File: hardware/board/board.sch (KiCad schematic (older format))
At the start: 64 parts, among them J1 Power, J10 OUT B3, J12 IN C, J13 OUT C1, J14 OUT C2, J15 OUT C3, J17 OUT D, J18 IN D1, J19 IN D2, J2 IN A, J20 IN D3, J3 OUT A1, J4 OUT A2, J5 OUT A3, J7 IN B, J8 OUT B1, J9 OUT B2, U1 OPA4991, U2 OPA4991, U4 OPA4991, U6 OPA4991

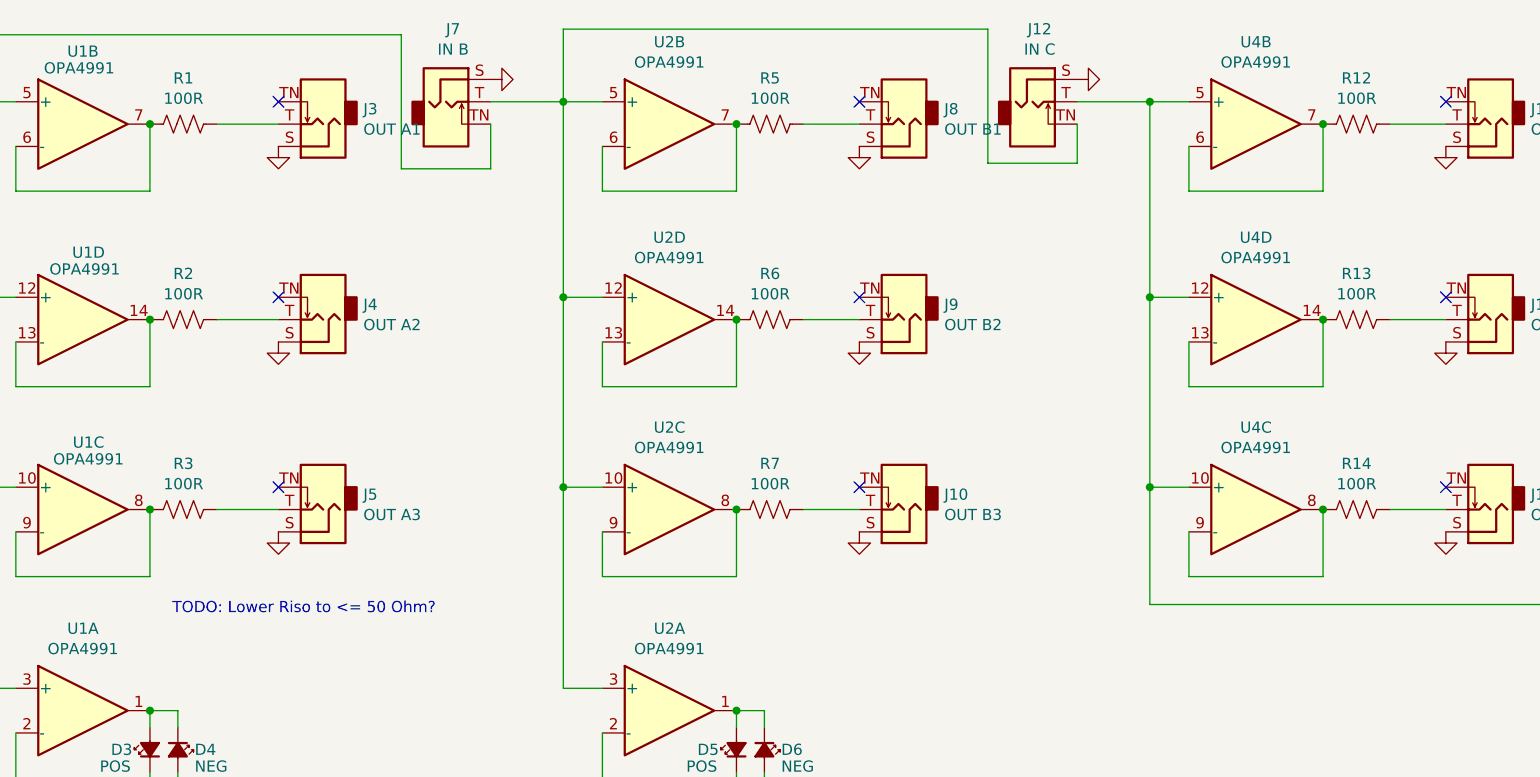
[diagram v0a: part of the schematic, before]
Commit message: Update resistor values; create PDF
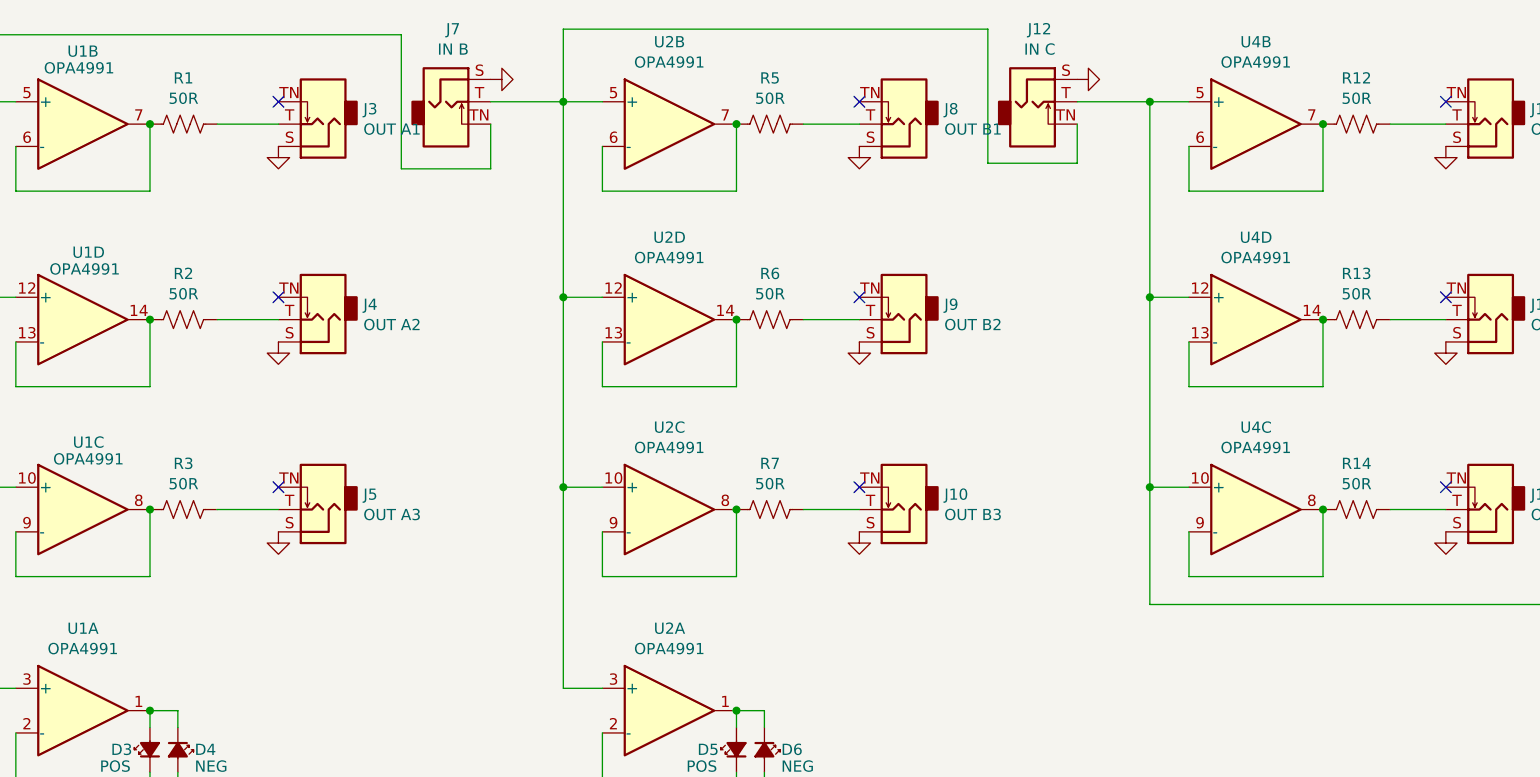
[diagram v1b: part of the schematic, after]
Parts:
- R1, R12, R13, R14, R2, R3, R5, R6, R7: value 100R -> 50R; Notes thin film -> thin film, highest possible wattage for size; mpn R0816P-101-D -> (none)
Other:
- note removed: "TODO: Lower Riso to <= 50 Ohm?"
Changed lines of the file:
@@
 P 2075 975
 F 0 "R1" V 1870 975 50  0000 C CNN
-F 1 "100R" V 1961 975 50  0000 C CNN
+F 1 "50R" V 1961 975 50  0000 C CNN
 F 2 "Resistor_SMD:R_0603_1608Metric_Pad0.98x0.95mm_HandSolder" V 2115 965 50  0001 C CNN
 F 3 "~" H 2075 975 50  0001 C CNN
-F 4 "R0816P-101-D" H 2075 975 50  0001 C CNN "mpn"
-F 5 "thin film" H 2075 975 50  0001 C CNN "Notes"
+F 4 "" H 2075 975 50  0001 C CNN "mpn"
+F 5 "thin film, highest possible wattage for size" H 2075 975 50  0001 C CNN "Notes"
 	1    2075 975
 	0    1    1    0
@@
 P 2075 1850
 F 0 "R2" V 1870 1850 50  0000 C CNN
-F 1 "100R" V 1961 1850 50  0000 C CNN
+F 1 "50R" V 1961 1850 50  0000 C CNN
 F 2 "Resistor_SMD:R_0603_1608Metric_Pad0.98x0.95mm_HandSolder" V 2115 1840 50  0001 C CNN
 F 3 "~" H 2075 1850 50  0001 C CNN
-F 4 "R0816P-101-D" H 2075 1850 50  0001 C CNN "mpn"
-F 5 "thin film" H 2075 1850 50  0001 C CNN "Notes"
+F 4 "" H 2075 1850 50  0001 C CNN "mpn"
+F 5 "thin film, highest possible wattage for size" H 2075 1850 50  0001 C CNN "Notes"
 	1    2075 1850
 	0    1    1    0
@@
 P 2075 2700
 F 0 "R3" V 1870 2700 50  0000 C CNN
-F 1 "100R" V 1961 2700 50  0000 C CNN
+F 1 "50R" V 1961 2700 50  0000 C CNN
 F 2 "Resistor_SMD:R_0603_1608Metric_Pad0.98x0.95mm_HandSolder" V 2115 2690 50  0001 C CNN
 F 3 "~" H 2075 2700 50  0001 C CNN
-F 4 "R0816P-101-D" H 2075 2700 50  0001 C CNN "mpn"
-F 5 "thin film" H 2075 2700 50  0001 C CNN "Notes"
+F 4 "" H 2075 2700 50  0001 C CNN "mpn"
+F 5 "thin film, highest possible wattage for size" H 2075 2700 50  0001 C CNN "Notes"
 	1    2075 2700
 	0    1    1    0
@@
 P 4700 975
 F 0 "R5" V 4495 975 50  0000 C CNN
-F 1 "100R" V 4586 975 50  0000 C CNN
+F 1 "50R" V 4586 975 50  0000 C CNN
 F 2 "Resistor_SMD:R_0603_1608Metric_Pad0.98x0.95mm_HandSolder" V 4740 965 50  0001 C CNN
 F 3 "~" H 4700 975 50  0001 C CNN
-F 4 "R0816P-101-D" H 4700 975 50  0001 C CNN "mpn"
-F 5 "thin film" H 4700 975 50  0001 C CNN "Notes"
+F 4 "" H 4700 975 50  0001 C CNN "mpn"
+F 5 "thin film, highest possible wattage for size" H 4700 975 50  0001 C CNN "Notes"
 	1    4700 975
 	0    1    1    0
@@
 P 4700 1850
 F 0 "R6" V 4495 1850 50  0000 C CNN
-F 1 "100R" V 4586 1850 50  0000 C CNN
+F 1 "50R" V 4586 1850 50  0000 C CNN
 F 2 "Resistor_SMD:R_0603_1608Metric_Pad0.98x0.95mm_HandSolder" V 4740 1840 50  0001 C CNN
 F 3 "~" H 4700 1850 50  0001 C CNN
-F 4 "R0816P-101-D" H 4700 1850 50  0001 C CNN "mpn"
-F 5 "thin film" H 4700 1850 50  0001 C CNN "Notes"
+F 4 "" H 4700 1850 50  0001 C CNN "mpn"
+F 5 "thin film, highest possible wattage for size" H 4700 1850 50  0001 C CNN "Notes"
 	1    4700 1850
 	0    1    1    0
@@
 P 4700 2700
 F 0 "R7" V 4495 2700 50  0000 C CNN
-F 1 "100R" V 4586 2700 50  0000 C CNN
+F 1 "50R" V 4586 2700 50  0000 C CNN
 F 2 "Resistor_SMD:R_0603_1608Metric_Pad0.98x0.95mm_HandSolder" V 4740 2690 50  0001 C CNN
 F 3 "~" H 4700 2700 50  0001 C CNN
-F 4 "R0816P-101-D" H 4700 2700 50  0001 C CNN "mpn"
-F 5 "thin film" H 4700 2700 50  0001 C CNN "Notes"
+F 4 "" H 4700 2700 50  0001 C CNN "mpn"
+F 5 "thin film, highest possible wattage for size" H 4700 2700 50  0001 C CNN "Notes"
 	1    4700 2700
 	0    1    1    0
@@
 P 7325 975
 F 0 "R12" V 7120 975 50  0000 C CNN
-F 1 "100R" V 7211 975 50  0000 C CNN
+F 1 "50R" V 7211 975 50  0000 C CNN
 F 2 "Resistor_SMD:R_0603_1608Metric_Pad0.98x0.95mm_HandSolder" V 7365 965 50  0001 C CNN
 F 3 "~" H 7325 975 50  0001 C CNN
-F 4 "R0816P-101-D" H 7325 975 50  0001 C CNN "mpn"
-F 5 "thin film" H 7325 975 50  0001 C CNN "Notes"
+F 4 "" H 7325 975 50  0001 C CNN "mpn"
+F 5 "thin film, highest possible wattage for size" H 7325 975 50  0001 C CNN "Notes"
 	1    7325 975
 	0    1    1    0
@@
 P 7325 1850
 F 0 "R13" V 7120 1850 50  0000 C CNN
-F 1 "100R" V 7211 1850 50  0000 C CNN
+F 1 "50R" V 7211 1850 50  0000 C CNN
 F 2 "Resistor_SMD:R_0603_1608Metric_Pad0.98x0.95mm_HandSolder" V 7365 1840 50  0001 C CNN
 F 3 "~" H 7325 1850 50  0001 C CNN
-F 4 "R0816P-101-D" H 7325 1850 50  0001 C CNN "mpn"
-F 5 "thin film" H 7325 1850 50  0001 C CNN "Notes"
+F 4 "" H 7325 1850 50  0001 C CNN "mpn"
+F 5 "thin film, highest possible wattage for size" H 7325 1850 50  0001 C CNN "Notes"
 	1    7325 1850
 	0    1    1    0
@@
 P 7325 2700
 F 0 "R14" V 7120 2700 50  0000 C CNN
-F 1 "100R" V 7211 2700 50  0000 C CNN
+F 1 "50R" V 7211 2700 50  0000 C CNN
 F 2 "Resistor_SMD:R_0603_1608Metric_Pad0.98x0.95mm_HandSolder" V 7365 2690 50  0001 C CNN
 F 3 "~" H 7325 2700 50  0001 C CNN
-F 4 "R0816P-101-D" H 7325 2700 50  0001 C CNN "mpn"
-F 5 "thin film" H 7325 2700 50  0001 C CNN "Notes"
+F 4 "" H 7325 2700 50  0001 C CNN "mpn"
+F 5 "thin film, highest possible wattage for size" H 7325 2700 50  0001 C CNN "Notes"
 	1    7325 2700
 	0    1    1    0
@@
 	3325 6800 3175 6800
 Connection ~ 3325 6800
-Text Notes 2025 3175 0    50   ~ 0
-TODO: Lower Riso to <= 50 Ohm?
 Text Notes 8400 5550 0    50   ~ 0
 C11 creates a low-pass filter\n- Fc @ 132kHz w/ 12pF\n- Fc @ 88kHz w/ 18pF

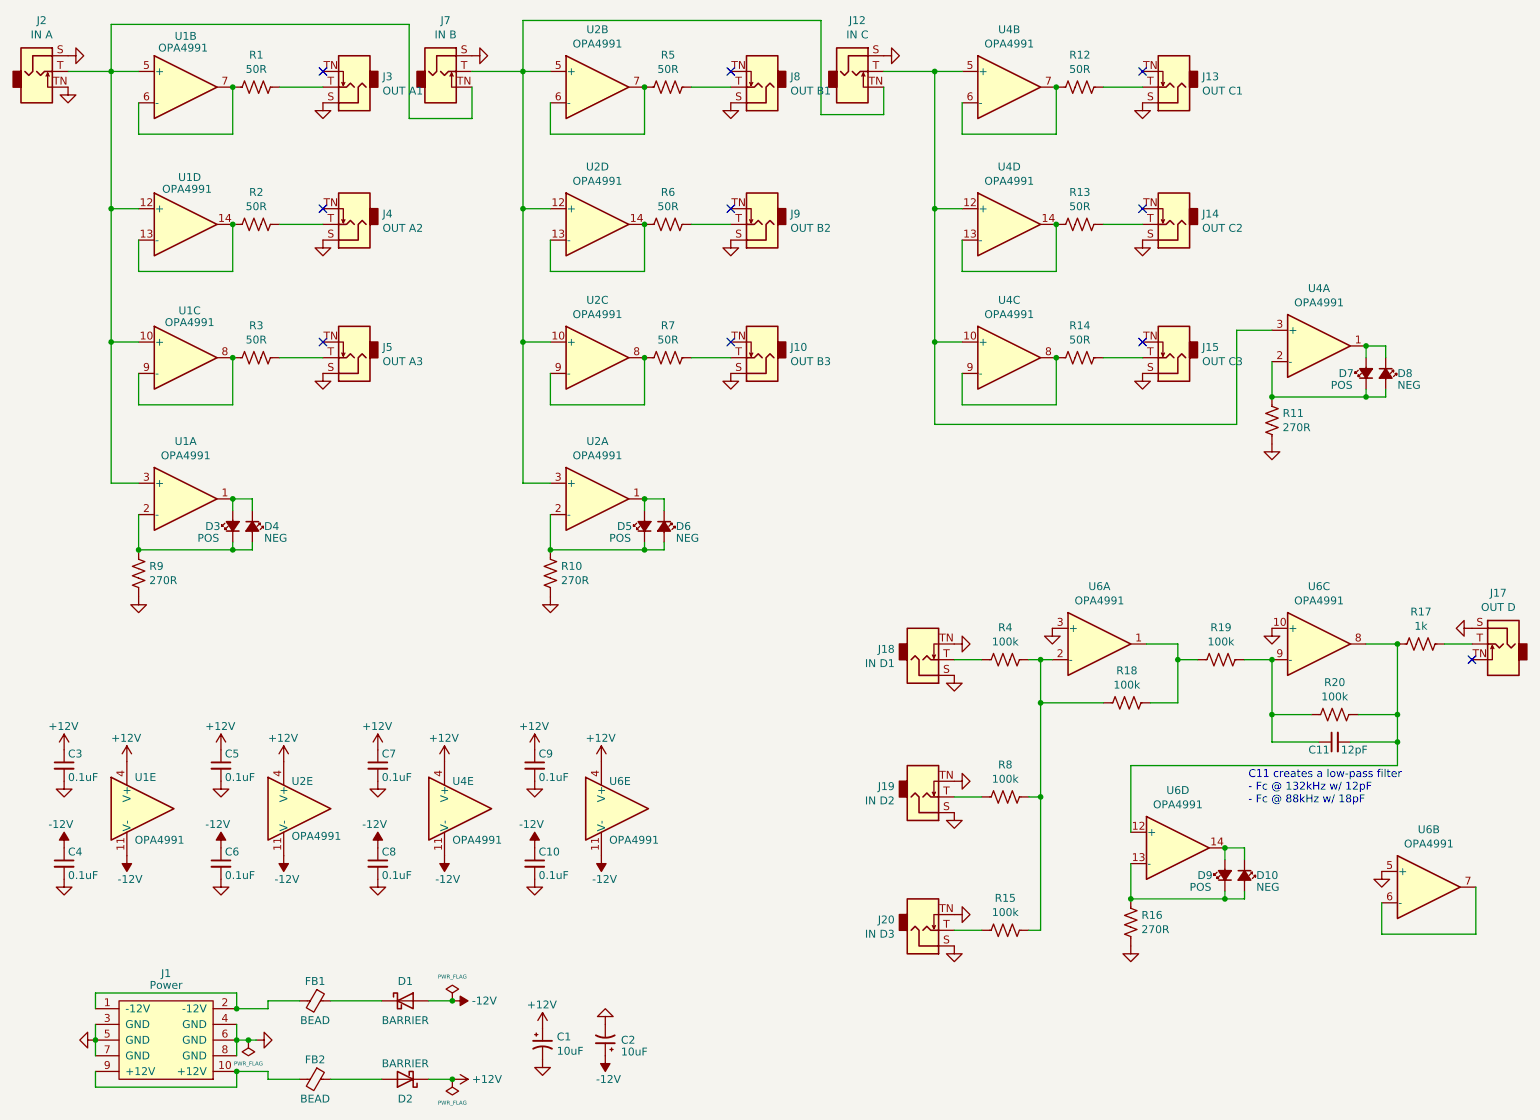
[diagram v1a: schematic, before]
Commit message: Update values for resistors
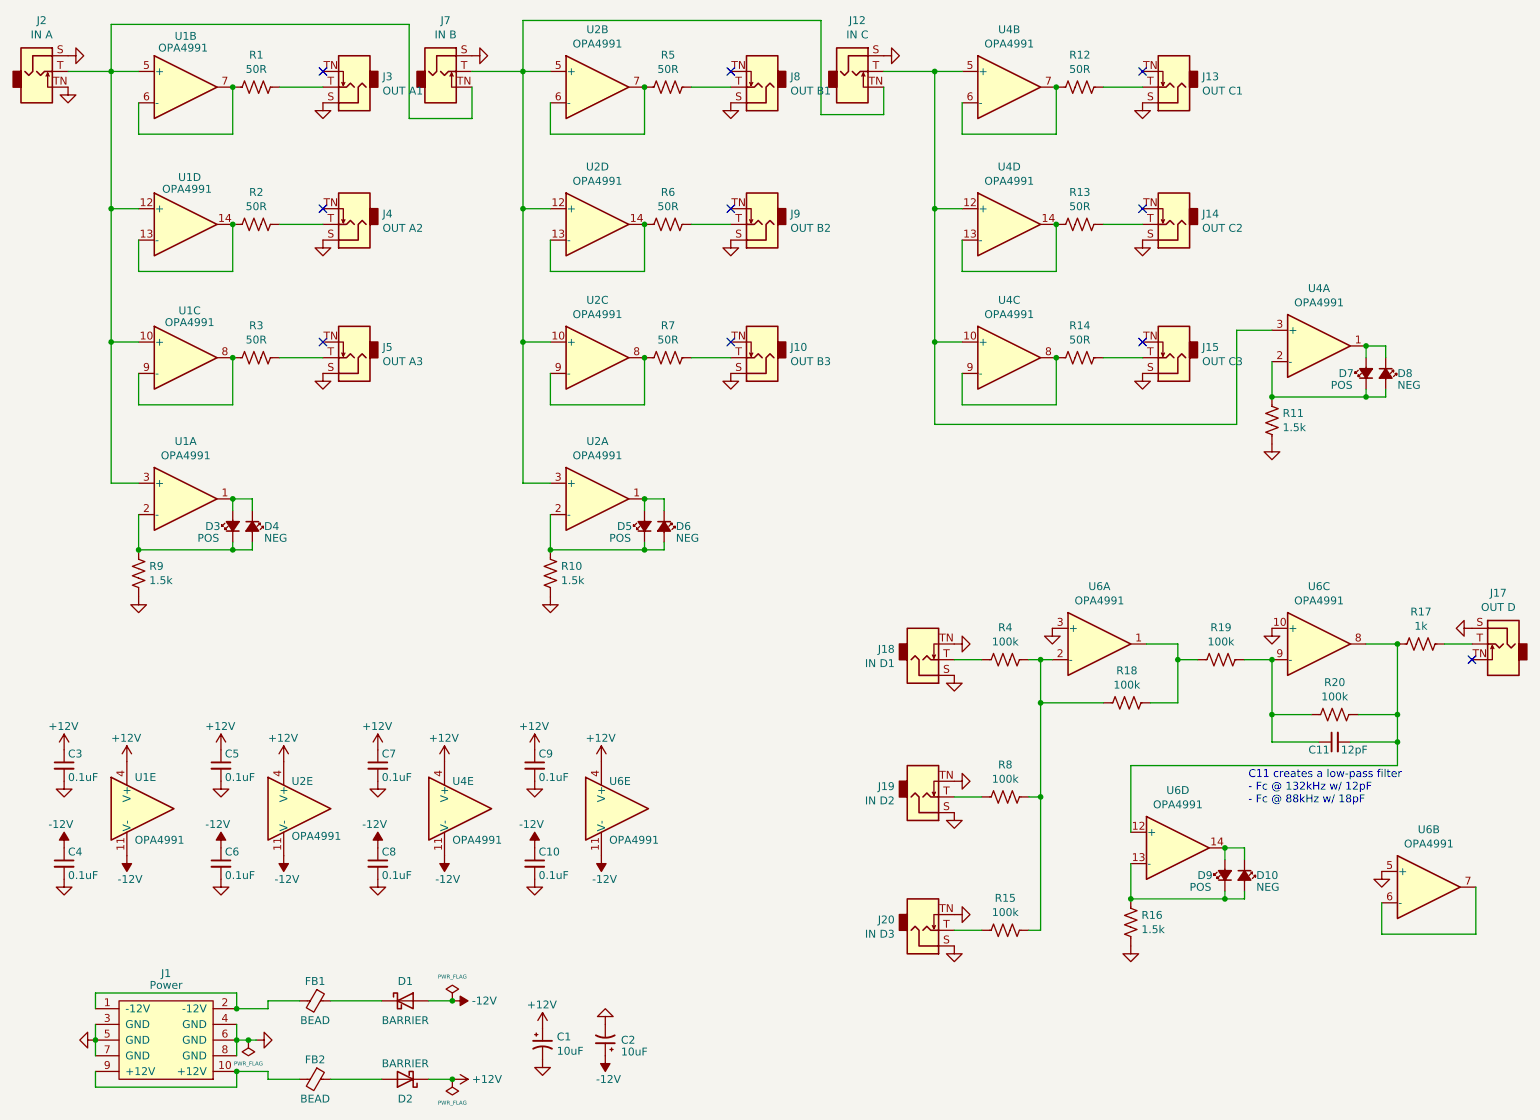
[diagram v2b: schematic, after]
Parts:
- R10, R11, R16, R9: value 270R -> 1.5k; mpn ERJ-3GEYJ271V -> ERJ-3GEYJ1R5V
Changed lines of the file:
@@
 P 1325 4075
 F 0 "R9" H 1257 4029 50  0000 R CNN
-F 1 "270R" H 1257 4120 50  0000 R CNN
+F 1 "1.5k" H 1257 4120 50  0000 R CNN
 F 2 "Resistor_SMD:R_0603_1608Metric_Pad0.98x0.95mm_HandSolder" V 1365 4065 50  0001 C CNN
 F 3 "~" H 1325 4075 50  0001 C CNN
-F 4 "ERJ-3GEYJ271V" H 1325 4075 50  0001 C CNN "mpn"
+F 4 "ERJ-3GEYJ1R5V" H 1325 4075 50  0001 C CNN "mpn"
 F 5 "" H 1325 4075 50  0001 C CNN "unit cost"
 F 6 "5%, thick film" H 1325 4075 50  0001 C CNN "Notes"
@@
 P 3950 4075
 F 0 "R10" H 3882 4029 50  0000 R CNN
-F 1 "270R" H 3882 4120 50  0000 R CNN
+F 1 "1.5k" H 3882 4120 50  0000 R CNN
 F 2 "Resistor_SMD:R_0603_1608Metric_Pad0.98x0.95mm_HandSolder" V 3990 4065 50  0001 C CNN
 F 3 "~" H 3950 4075 50  0001 C CNN
-F 4 "ERJ-3GEYJ271V" H 3950 4075 50  0001 C CNN "mpn"
+F 4 "ERJ-3GEYJ1R5V" H 3950 4075 50  0001 C CNN "mpn"
 F 5 "" H 3950 4075 50  0001 C CNN "unit cost"
 F 6 "5%, thick film" H 3950 4075 50  0001 C CNN "Notes"
@@
 P 8550 3100
 F 0 "R11" H 8482 3054 50  0000 R CNN
-F 1 "270R" H 8482 3145 50  0000 R CNN
+F 1 "1.5k" H 8482 3145 50  0000 R CNN
 F 2 "Resistor_SMD:R_0603_1608Metric_Pad0.98x0.95mm_HandSolder" V 8590 3090 50  0001 C CNN
 F 3 "~" H 8550 3100 50  0001 C CNN
-F 4 "ERJ-3GEYJ271V" H 8550 3100 50  0001 C CNN "mpn"
+F 4 "ERJ-3GEYJ1R5V" H 8550 3100 50  0001 C CNN "mpn"
 F 5 "" H 8550 3100 50  0001 C CNN "unit cost"
 F 6 "5%, thick film" H 8550 3100 50  0001 C CNN "Notes"
@@
 P 7650 6300
 F 0 "R16" H 7582 6254 50  0000 R CNN
-F 1 "270R" H 7582 6345 50  0000 R CNN
+F 1 "1.5k" H 7582 6345 50  0000 R CNN
 F 2 "Resistor_SMD:R_0603_1608Metric_Pad0.98x0.95mm_HandSolder" V 7690 6290 50  0001 C CNN
 F 3 "~" H 7650 6300 50  0001 C CNN
-F 4 "ERJ-3GEYJ271V" H 7650 6300 50  0001 C CNN "mpn"
+F 4 "ERJ-3GEYJ1R5V" H 7650 6300 50  0001 C CNN "mpn"
 F 5 "" H 7650 6300 50  0001 C CNN "unit cost"
 F 6 "5%, thick film" H 7650 6300 50  0001 C CNN "Notes"

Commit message: user guide: Add surface mount kit assembly guide
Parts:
- C1, C10, C11, C2, C3, C4, C5, C6, C7, C8, C9, D1, D10, D2, D3, D4, D5, D6, D7, D8, D9, FB1, FB2, R1, R10, R11, R12, R13, R14, R15, R16, R17, R18, R19, R2, R20, R3, R4, R5, R6, R7, R8, R9, U1, U2, U4, U6: smd kit (none) -> 1
